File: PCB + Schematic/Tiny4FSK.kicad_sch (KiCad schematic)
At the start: 77 parts, among them IC1 SI4063, J1 SWD, J2 GPIO, J3 USBC, J4 OPTIONAL, J5 I2C, J6 Power, J7 SPI, SW1 RST, SW2 BATT PWR, U1 ATSAMD21G18A-A, U2 MAX-M10S, U2 TPS61200DRC, U5 TCXO MCU, U8 Linear Step-Down

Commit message: Rebase Rev. 4 PCB files
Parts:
- removed BT2: AAA, BatteryExtended:BAT_BK-82, symbol Device:Battery_Cell
- removed C11: 100 pF, Capacitor_SMD:C_0805_2012Metric_Pad1.18x1.45mm_HandSolder, symbol Device:C_Small
- removed C2: 100 nF, Capacitor_SMD:C_0805_2012Metric_Pad1.18x1.45mm_HandSolder, symbol Device:C_Small
- removed C23 (x2): 1uF, Capacitor_SMD:C_0805_2012Metric_Pad1.18x1.45mm_HandSolder, symbol Device:C_Small
- removed C7: 4.5 nF, Capacitor_SMD:C_0805_2012Metric_Pad1.18x1.45mm_HandSolder, symbol Device:C_Small
- removed J3: USBC, Connector_USB:USB_C_Receptacle_GCT_USB4105-xx-A_16P_TopMnt_Horizontal, symbol Connector:USB_C_Receptacle_USB2.0
- removed J4: OPTIONAL, Jumper:SolderJumper-2_P1.3mm_Open_Pad1.0x1.5mm, symbol Connector_Generic:Conn_01x02
- removed JP2: Source, Jumper:SolderJumper-3_P1.3mm_Open_Pad1.0x1.5mm_NumberLabels, symbol Jumper:Jumper_3_Open
- removed R3: 1M, Resistor_SMD:R_0805_2012Metric_Pad1.20x1.40mm_HandSolder, symbol Device:R_Small_US
- removed R7: 5k1, Resistor_SMD:R_0805_2012Metric_Pad1.20x1.40mm_HandSolder, symbol Device:R_Small_US
- removed U8: Linear Step-Down, Package_TO_SOT_SMD:SOT-89-3_Handsoldering, symbol Regulator_Linear:MCP1700x-330xxTT
- added BT1: BK-53, BatteryExtended:BAT_53, symbol Device:Battery_Cell
- added C13, C29: 100nF, Capacitor_SMD:C_0402_1005Metric_Pad0.74x0.62mm_HandSolder, symbol Device:C_Small
- added C17, C25, C30: 100 nF, Capacitor_SMD:C_0402_1005Metric_Pad0.74x0.62mm_HandSolder, symbol Device:C_Small
- added C18: 1uF, Capacitor_SMD:C_0402_1005Metric_Pad0.74x0.62mm_HandSolder, symbol Device:C_Small
- added C19: 4.7 nF, Capacitor_SMD:C_0402_1005Metric_Pad0.74x0.62mm_HandSolder, symbol Device:C_Small
- added C28: 1.5pF, Capacitor_SMD:C_0402_1005Metric_Pad0.74x0.62mm_HandSolder, symbol Device:C_Small
- added J4: USB, Connector_PinHeader_2.54mm:PinHeader_1x04_P2.54mm_Vertical, symbol Connector_Generic:Conn_01x04
- added J5: USB Breakout, Connector_PinHeader_2.54mm:PinHeader_1x04_P2.54mm_Vertical, symbol Connector_Generic:Conn_01x04
- added J7: USBC, Connector_USB:USB_C_Receptacle_GCT_USB4105-xx-A_16P_TopMnt_Horizontal, symbol Connector:USB_C_Receptacle_USB2.0
- added L8: 3.9 nH, Inductor_SMD:L_0402_1005Metric_Pad0.77x0.64mm_HandSolder, symbol Device:L
- added R10, R12: 5k1, Resistor_SMD:R_0402_1005Metric_Pad0.72x0.64mm_HandSolder, symbol Device:R_Small_US
- added R11, R6: 1M, Resistor_SMD:R_0402_1005Metric_Pad0.72x0.64mm_HandSolder, symbol Device:R_Small_US
- added U7: Linear Step-Down, LDO:MCP1700, symbol Regulator_Linear:MCP1700x-330xxTT
- #C9, C21, C22, C7: footprint Capacitor_SMD:C_0805_2012Metric_Pad1.18x1.45mm_HandSolder -> Capacitor_SMD:C_0402_1005Metric_Pad0.74x0.62mm_HandSolder; LCSC (none) -> C52923
- #U6: LCSC (none) -> C92489
- AE1: value GPS ANT -> 1575AT43A0040; LCSC (none) -> C239243
- AE2: value ANT -> TX Antenna; now not fitted
- C1: value 100 nF -> 10uF; footprint Capacitor_SMD:C_0805_2012Metric_Pad1.18x1.45mm_HandSolder -> Capacitor_SMD:C_0402_1005Metric_Pad0.74x0.62mm_HandSolder; LCSC (none) -> C19702
- C14: footprint Capacitor_SMD:C_0805_2012Metric_Pad1.18x1.45mm_HandSolder -> Capacitor_SMD:C_0402_1005Metric_Pad0.74x0.62mm_HandSolder; LCSC (none) -> C19702
- C15: footprint Capacitor_SMD:C_0805_2012Metric_Pad1.18x1.45mm_HandSolder -> Capacitor_SMD:C_0603_1608Metric_Pad1.08x0.95mm_HandSolder; LCSC (none) -> C59461
- C15: renamed from C19; LCSC (none) -> C161337
- C16: renamed from C20; footprint Capacitor_SMD:C_0603_1608Metric_Pad1.08x0.95mm_HandSolder -> Capacitor_SMD:C_0402_1005Metric_Pad0.74x0.62mm_HandSolder; LCSC (none) -> C1525
- C16, C19, C6: footprint Capacitor_SMD:C_0805_2012Metric_Pad1.18x1.45mm_HandSolder -> Capacitor_SMD:C_0402_1005Metric_Pad0.74x0.62mm_HandSolder; LCSC (none) -> C1525
- C2: value 10uF -> 100 nF; footprint Capacitor_SMD:C_0805_2012Metric_Pad1.18x1.45mm_HandSolder -> Capacitor_SMD:C_0402_1005Metric_Pad0.74x0.62mm_HandSolder; LCSC (none) -> C1525
- C20: renamed from C22; value 15 pF -> 8 pF; footprint Capacitor_SMD:C_0201_0603Metric_Pad0.64x0.40mm_HandSolder -> Capacitor_SMD:C_0402_1005Metric_Pad0.74x0.62mm_HandSolder; LCSC (none) -> C1548
- C21: renamed from C23; footprint Capacitor_SMD:C_0805_2012Metric_Pad1.18x1.45mm_HandSolder -> Capacitor_SMD:C_0402_1005Metric_Pad0.74x0.62mm_HandSolder; LCSC (none) -> C1546
- C21: value 10 nF -> 100 nF; footprint Capacitor_SMD:C_0805_2012Metric_Pad1.18x1.45mm_HandSolder -> Capacitor_SMD:C_0402_1005Metric_Pad0.74x0.62mm_HandSolder; LCSC (none) -> C1525
- C23: renamed from C18; footprint Capacitor_SMD:C_0805_2012Metric_Pad1.18x1.45mm_HandSolder -> Capacitor_SMD:C_0402_1005Metric_Pad0.74x0.62mm_HandSolder; LCSC (none) -> C1525
- C24: renamed from C25; value 12 pF -> 6 pF; LCSC (none) -> C1547
- C27: value 10 pF -> 5 pF; footprint Capacitor_SMD:C_0201_0603Metric_Pad0.64x0.40mm_HandSolder -> Capacitor_SMD:C_0402_1005Metric_Pad0.74x0.62mm_HandSolder; LCSC (none) -> C32949
- C4: value 100nF -> 10 uF; footprint Capacitor_SMD:C_0805_2012Metric_Pad1.18x1.45mm_HandSolder -> Capacitor_SMD:C_0402_1005Metric_Pad0.74x0.62mm_HandSolder; LCSC (none) -> C19702
- C5: value 100nF -> 100 nF; footprint Capacitor_SMD:C_0805_2012Metric_Pad1.18x1.45mm_HandSolder -> Capacitor_SMD:C_0402_1005Metric_Pad0.74x0.62mm_HandSolder; LCSC (none) -> C1525
- C9: value 100nF -> 10 uF; footprint Capacitor_SMD:C_0805_2012Metric_Pad1.18x1.45mm_HandSolder -> Capacitor_SMD:C_0603_1608Metric_Pad1.08x0.95mm_HandSolder; LCSC (none) -> C19702
- D1: LCSC (none) -> C2297
- D2, D3: LCSC (none) -> C84256
- FB1: LCSC (none) -> C76892
- J1: renamed from J6; value Power -> Power Ext; now not fitted
- J2: now not fitted
- J3: renamed from J5; now not fitted
- J6: renamed from J7; now not fitted
- J8: renamed from J1; footprint Connector_PinHeader_2.54mm:PinHeader_1x06_P2.54mm_Vertical -> Connector_PinHeader_1.27mm:PinHeader_2x05_P1.27mm_Vertical_SMD; symbol Connector_Generic:Conn_01x06 -> Connector_Generic:Conn_02x05_Odd_Even; now not fitted
- JP1: value SWITCH_EN -> Switch EN; now not fitted
- L1: value 33 nH -> 3.9 nH; LCSC (none) -> C307609
- L2: LCSC (none) -> C2844756
- L3: footprint Inductor_SMD:L_0603_1608Metric_Pad1.05x0.95mm_HandSolder -> Inductor_SMD:L_0402_1005Metric_Pad0.77x0.64mm_HandSolder; LCSC (none) -> C275307
- L4: value 33 nH -> 14 nH; LCSC (none) -> C307609
- L5: value 30 nH -> 14 nH; LCSC (none) -> C341687
- L6: value 36 nH -> 14 nH; LCSC (none) -> C167476
- L7: value 22 nH -> 14 nH; LCSC (none) -> C86129
- R1: renamed from R2; footprint Resistor_SMD:R_0805_2012Metric_Pad1.20x1.40mm_HandSolder -> Resistor_SMD:R_0402_1005Metric_Pad0.72x0.64mm_HandSolder; LCSC (none) -> C25744
- R13: renamed from R10; value 100 -> 330; footprint Resistor_SMD:R_0805_2012Metric_Pad1.20x1.40mm_HandSolder -> Resistor_SMD:R_0402_1005Metric_Pad0.72x0.64mm_HandSolder; LCSC (none) -> C23138
- R14: renamed from R13; value 1k -> 330; footprint Resistor_SMD:R_0805_2012Metric_Pad1.20x1.40mm_HandSolder -> Resistor_SMD:R_0402_1005Metric_Pad0.72x0.64mm_HandSolder; LCSC (none) -> C23138
- R15: renamed from R9; value 100 -> 330; footprint Resistor_SMD:R_0805_2012Metric_Pad1.20x1.40mm_HandSolder -> Resistor_SMD:R_0402_1005Metric_Pad0.72x0.64mm_HandSolder; LCSC (none) -> C23138
- R2: renamed from R1; footprint Resistor_SMD:R_0805_2012Metric_Pad1.20x1.40mm_HandSolder -> Resistor_SMD:R_0402_1005Metric_Pad0.72x0.64mm_HandSolder; LCSC (none) -> C25744
- R3: renamed from R12; value 5M -> 1M; footprint Resistor_SMD:R_0805_2012Metric_Pad1.20x1.40mm_HandSolder -> Resistor_SMD:R_0402_1005Metric_Pad0.72x0.64mm_HandSolder; LCSC (none) -> C26083
- R4: renamed from R11; value 900k -> 180k; footprint Resistor_SMD:R_0805_2012Metric_Pad1.20x1.40mm_HandSolder -> Resistor_SMD:R_0402_1005Metric_Pad0.72x0.64mm_HandSolder; LCSC (none) -> C100276
- R5: value 5k1 -> 1M; footprint Resistor_SMD:R_0805_2012Metric_Pad1.20x1.40mm_HandSolder -> Resistor_SMD:R_0402_1005Metric_Pad0.72x0.64mm_HandSolder; LCSC (none) -> C26083
- R7: renamed from R4; footprint Resistor_SMD:R_0805_2012Metric_Pad1.20x1.40mm_HandSolder -> Resistor_SMD:R_0402_1005Metric_Pad0.72x0.64mm_HandSolder; LCSC (none) -> C25091
- R8: renamed from R6; footprint Resistor_SMD:R_0805_2012Metric_Pad1.20x1.40mm_HandSolder -> Resistor_SMD:R_0402_1005Metric_Pad0.72x0.64mm_HandSolder; LCSC (none) -> C4177
- R9: renamed from R8; footprint Resistor_SMD:R_0805_2012Metric_Pad1.20x1.40mm_HandSolder -> Resistor_SMD:R_0402_1005Metric_Pad0.72x0.64mm_HandSolder; LCSC (none) -> C4177
- SW1: LCSC (none) -> C2888954
- SW1: renamed from SW2; value BATT PWR -> Power Switch; footprint SlideSwitch:WS-SLSU_6p7x2p7_WRE -> Button_Switch_SMD:SW_SPDT_PCM12; LCSC (none) -> C963206
- U1: LCSC (none) -> C78624
- U2: LCSC (none) -> C140320
- U2: value MAX-M10S -> ATGM336H; footprint RF_GPS:ublox_MAX -> RF_GPS_Extended:ATGM336H; symbol RF_GPS:MAX-M10S -> RF_GPS_Extended:ATGM336H; LCSC (none) -> C5117921
- U4: renamed from U5; value TCXO MCU -> ECS-327TXO-2012; footprint Oscillator_TCXO:ATXK-H11-E-32.768KHZ-E50-T3 -> Oscillator_TCXO:ECS-327TXO-2012; LCSC (none) -> C213398
- U8: renamed from XTAL1; footprint OSC:OSC_ECS-TXO-32CSMV-260-AN-TR -> Oscillator_TCXO:ECS-TXO-20CSMV4; LCSC (none) -> C135223
- renumbered IC1 to U6
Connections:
- net BOOST is gone; now on net +3.3V: C15.1, C16.1, R3.1, U2.2 (VOUT)
- net LDO is gone; now on net Earth: C22.1
- net +3.3V: now also C1.2, D3.2 (A), R8.1, U2.6 (VBAT), C13.2, C18.1, C29.1, C30.2, J4.3 (Pin_3), J5.3 (Pin_3), U7.2 (VO); no longer R14.1, R8.2, U2.7 (VCC_IO)
- net +BATT: now also R5.1, BT1.1 (+); no longer U1.3 (PA02)
- net ANT_GPS: now also C28.1, L8.2; no longer AE1.1 (A), L1.2
- net D+: now also J4.1 (Pin_1), J5.1 (Pin_1), J7.A6 (D+), J7.B6 (D+)
- net D-: now also J4.2 (Pin_2), J5.2 (Pin_2), J7.A7 (D-), J7.B7 (D-)
- net ERROR: now also D2.2 (A); no longer R13.1
- net Earth: now also C1.1, R13.2, R14.2, R15.2, BT1.2 (-), C13.1, C17.2, C18.2, C19.1, C25.2, C29.2, C30.1, J4.4 (Pin_4), J5.4 (Pin_4), J7.A1 (GND), J7.A12 (GND), J7.B1 (GND), J7.B12 (GND), L8.1, R10.1, R11.2, R12.1, R6.2, U7.1 (GND); no longer C1.2, C22.2, D1.1 (K), D2.1 (K), D3.1 (K), R5.1
- net LIN: now also C22.2, C17.1, U7.3 (VI); no longer C1.1
- net SCL: now also R8.2; no longer R8.1, U2.17 (SCL)
- net SDA: no longer U2.16 (SDA)
- net SUCCESS: now also D1.2 (A); no longer R15.2
- net TCXO: now also U4.3 (OUTPUT)
- net USB: now also C25.1, J7.A4 (VBUS), J7.A9 (VBUS), J7.B4 (VBUS), J7.B9 (VBUS)
- net nRST: now also J8.10 (Pin_10); no longer J8.6 (Pin_6)
- net BATT_SENSE: now reaches R5.2
- net BATT_SENSE: now also U1.3 (PA02), R6.1
- net at R15.1: now also D1.1 (K); no longer D1.2 (A)
- net RXD: now reaches U2.2 (TXD)
- net RXD: now also U1.16 (PA11)
- net TXD: now reaches U2.3 (RXD)
- net TXD: now also U1.15 (PA10)
- net EXTINT renamed GPS_EN
- net OPT XOUT: no longer names the net of U1.2 (PA01)
- new net: D3.1 (K), R14.1
- new net: J7.B5 (CC2), R10.2
- new net: J7.A5 (CC1), R12.2
- new net: D2.1 (K), R13.1
- new net: AE1.1 (A), C28.2, L1.2
- new net: C19.2, J7.S1 (SHIELD), R11.1
- no-connect marks 0 -> 30
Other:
- note added: "Look into: SXBP-425+"
- note added: "SAMD21G18A MCU + Voltmeter"
- note removed: "SAMD21G18A MCU + Voltmeter + USB"
- note removed: "USB Step-Down Converter 5v -> 3.3v"
- moved on the sheet: AE1, C16, D1, D2, D3, L1, R13, R14, R15, R8, SW1, U4

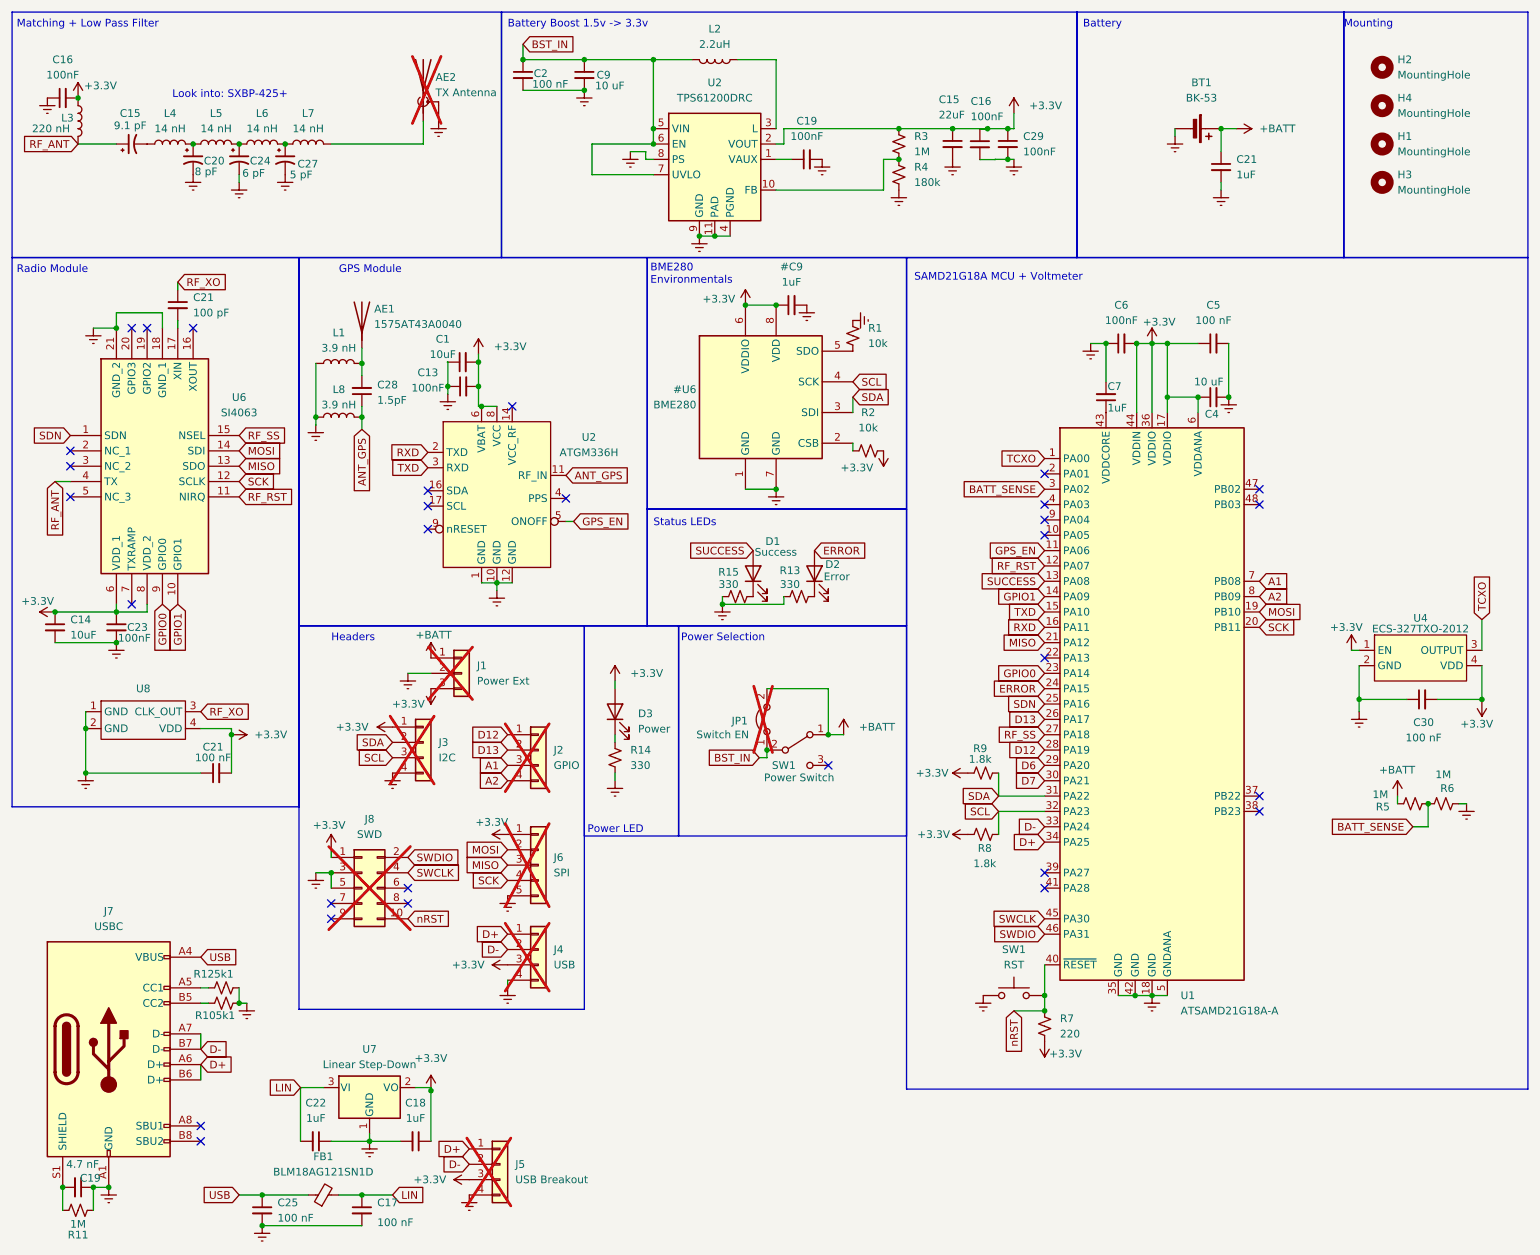
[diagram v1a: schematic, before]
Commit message: clean out sd code, adjust voltage formula
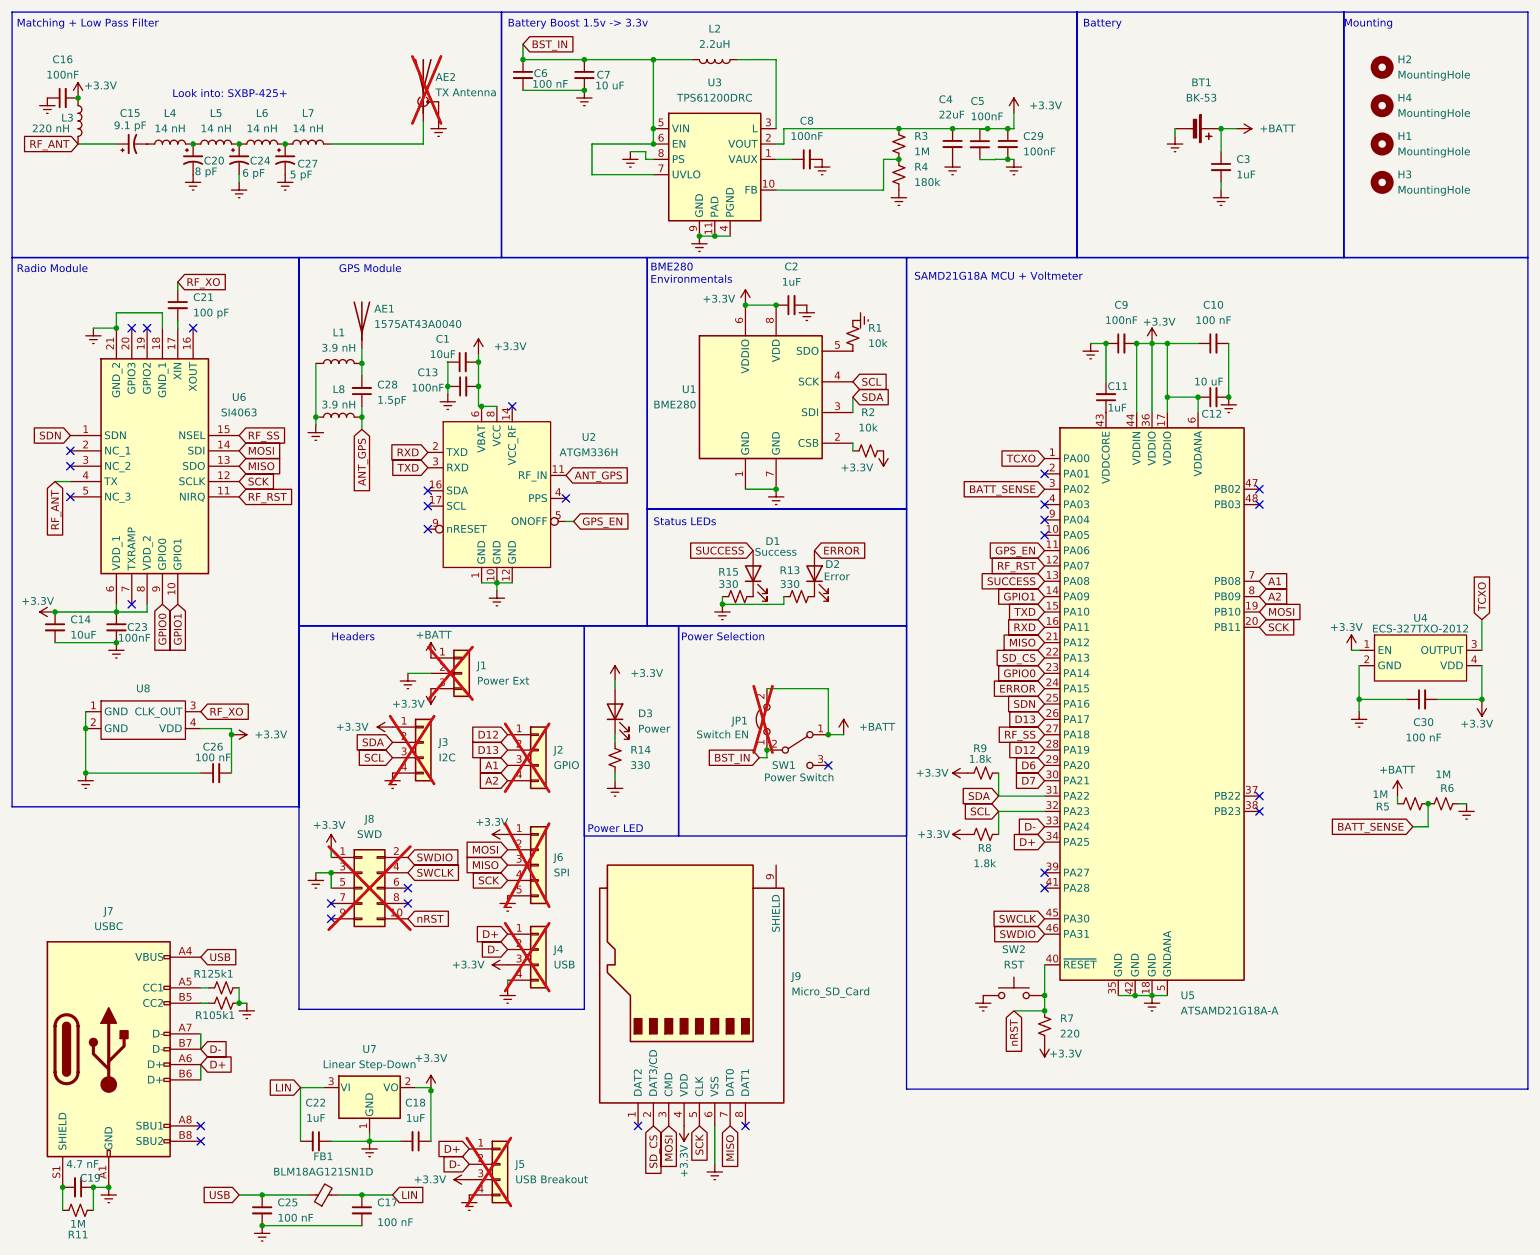
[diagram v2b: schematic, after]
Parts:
- added J9: Micro_SD_Card, symbol Connector:Micro_SD_Card
- renumbered C5 to C10, C7 to C11, C4 to C12, #C9 to C2, C21 to C26, C21 to C3, C15 to C4, C16 to C5, C2 to C6, C9 to C7, C19 to C8, C6 to C9, SW1 to SW2, #U6 to U1, U2 to U3, U1 to U5
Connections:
- net +3.3V: now also J9.4 (VDD)
- net Earth: now also J9.6 (VSS)
- net MISO: now also J9.7 (DAT0)
- net MOSI: now also J9.3 (CMD)
- net SCK: now also J9.5 (CLK)
- net SD_CS: now reaches U5.22 (PA13)
- net SD_CS: now also J9.2 (DAT3/CD)
- no-connect marks 30 -> 31

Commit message: revert kicad version to 8
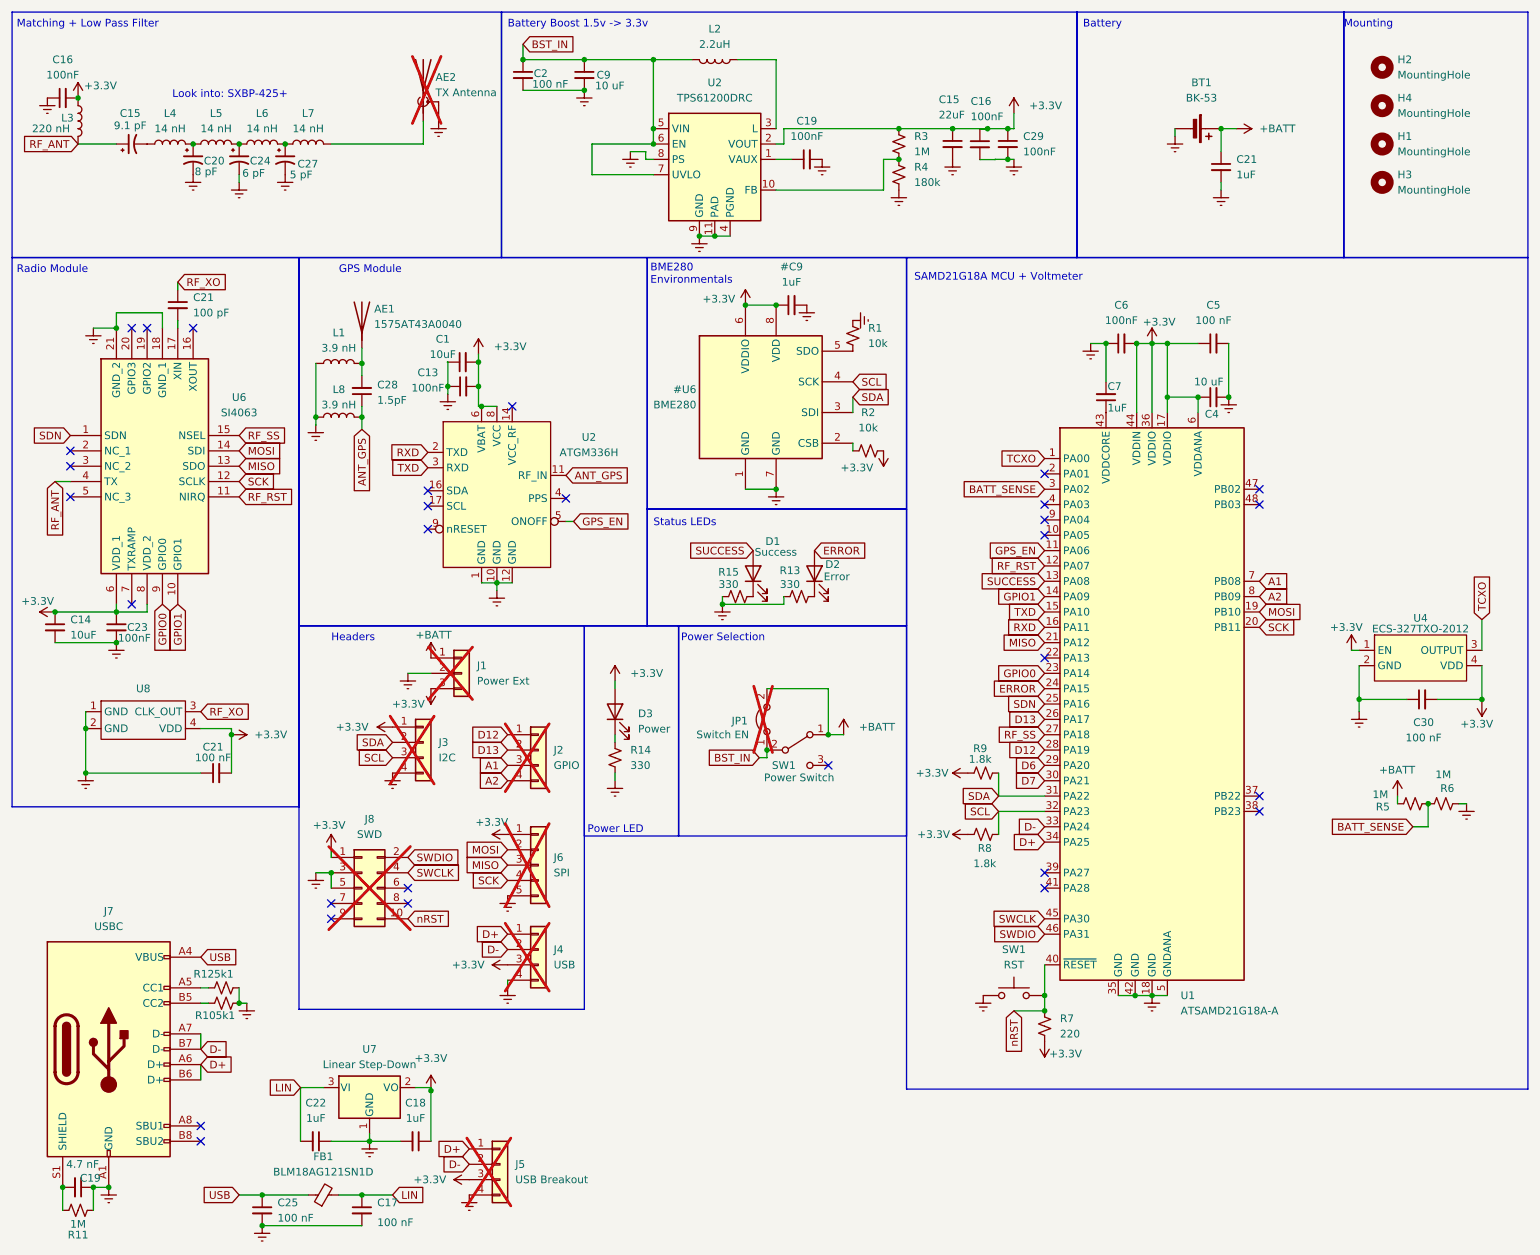
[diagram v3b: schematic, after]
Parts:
- removed J9: Micro_SD_Card, symbol Connector:Micro_SD_Card
- renumbered C2 to #C9, U1 to #U6, C4 to C15, C5 to C16, C8 to C19, C6 to C2, C3 to C21, C26 to C21, C12 to C4, C10 to C5, C9 to C6, C11 to C7, C7 to C9, SW2 to SW1, U5 to U1, U3 to U2
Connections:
- net SD_CS: no longer names the net of U1.22 (PA13)
- no-connect marks 31 -> 30
